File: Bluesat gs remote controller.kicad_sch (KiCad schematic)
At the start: 55 parts, among them J1 USB_C_Receptacle_USB2.0_16P, J2 Conn_01x02, J3 Conn_01x04, J4 Conn_01x04, J5 Conn_01x06, J6 Conn_01x02, SW1 Reset, SW2 Boot, SW3 AZ, SW4 EL, U1 MCP73831-2-OT, U2 AP2112K-3.3, U4 ESP32-S3-WROOM-1

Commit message: Fix battery switch placement and status LED wiring
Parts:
- added SW5: SW_SPDT, symbol Switch:SW_SPDT
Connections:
- net GND: now also C1.1, C3.1, R4.2, U2.1 (VIN), U2.3 (EN), SW5.1 (A); no longer R19.1, R20.1
- net VBAT: now also SW5.2 (B); no longer C1.1, C3.1, R4.2, U2.1 (VIN), U2.3 (EN)
- net LED_STAT1: now reaches U4.17 (IO9)
- net LED_STAT1: now also R19.1
- net LED_STAT2: now reaches U4.18 (IO10)
- net LED_STAT2: now also R20.1
- no-connect marks 2 -> 3
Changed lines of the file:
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@@
-	)
-	(junction
-		(at 113.03 88.9)
-		(diameter 0)
-		(color 0 0 0 0)
 	)
 	(junction
@@
 	)
 	(junction
-		(at 140.97 36.83)
-		(diameter 0)
-		(color 0 0 0 0)
-	)
-	(junction
 		(at 130.81 88.9)
-		(diameter 0)
-		(color 0 0 0 0)
-	)
-	(junction
-		(at 113.03 107.95)
 		(diameter 0)
 		(color 0 0 0 0)
@@
 	)
 	(no_connect
+		(at 85.09 73.66)
+	)
+	(no_connect
 		(at 43.18 82.55)
 	)
@@
 	(wire
 		(pts
-			(xy 106.68 107.95) (xy 113.03 107.95)
-		)
-		(stroke
-			(width 0)
-			(type default)
-		)
-	)
-	(wire
-		(pts
 			(xy 27.94 92.71) (xy 27.94 99.06)
 		)
@@
 	(wire
 		(pts
-			(xy 113.03 88.9) (xy 125.73 88.9)
+			(xy 102.87 88.9) (xy 125.73 88.9)
 		)
 		(stroke
@@
 	(wire
 		(pts
-			(xy 113.03 107.95) (xy 120.65 107.95)
-		)
-		(stroke
-			(width 0)
-			(type default)
-		)
-	)
-	(wire
-		(pts
-			(xy 113.03 88.9) (xy 113.03 107.95)
-		)
-		(stroke
-			(width 0)
-			(type default)
-		)
-	)
-	(wire
-		(pts
 			(xy 148.59 88.9) (xy 148.59 97.79)
 		)
@@
 	(wire
 		(pts
-			(xy 102.87 88.9) (xy 113.03 88.9)
-		)
-		(stroke
-			(width 0)
-			(type default)
-		)
-	)
-	(wire
-		(pts
 			(xy 130.81 102.87) (xy 130.81 101.6)
 		)
@@
 	(wire
 		(pts
-			(xy 140.97 36.83) (xy 157.48 36.83)
+			(xy 134.62 36.83) (xy 157.48 36.83)
 		)
 		(stroke
@@
 	(wire
 		(pts
-			(xy 140.97 40.64) (xy 140.97 36.83)
-		)
-		(stroke
-			(width 0)
-			(type default)
-		)
-	)
-	(wire
-		(pts
 			(xy 140.97 48.26) (xy 140.97 53.34)
 		)
@@
 		(pts
 			(xy 146.05 158.75) (xy 153.67 158.75)
-		)
-		(stroke
-			(width 0)
-			(type default)
-		)
-	)
-	(wire
-		(pts
-			(xy 134.62 36.83) (xy 140.97 36.83)
 		)
 		(stroke
@@
 		)
 	)
+	(label "LED_STAT1"
+		(at 120.65 107.95 0)
+		(effects
+			(font
+				(size 1.27 1.27)
+			)
+			(justify left bottom)
+		)
+	)
 	(label "ENC_EL_A"
 		(at 207.01 137.16 0)
@@
 		)
 	)
+	(label "PWR_FLAG"
+		(at 60.96 88.9 90)
+		(effects
+			(font
+				(size 1.27 1.27)
+			)
+			(justify left bottom)
+		)
+	)
 	(label "USB_D-"
 		(at 63.5 127 180)
@@
 		)
 	)
+	(label "VSYS"
+		(at 85.09 68.58 0)
+		(effects
+			(font
+				(size 1.27 1.27)
+			)
+			(justify left bottom)
+		)
+	)
 	(label "5V"
 		(at 21.59 115.57 0)
@@
 		)
 	)
-	(label "VBAT"
-		(at 52.07 88.9 0)
+	(label "VSYS"
+		(at 52.07 88.9 180)
+		(effects
+			(font
+				(size 1.27 1.27)
+			)
+			(justify right bottom)
+		)
+	)
+	(label "VSYS"
+		(at 140.97 40.64 0)
 		(effects
 			(font
@@
 		)
 	)
+	(label "LED_STAT2"
+		(at 106.68 107.95 0)
+		(effects
+			(font
+				(size 1.27 1.27)
+			)
+			(justify left bottom)
+		)
+	)
 	(label "5V"
 		(at 123.19 63.5 0)
@@
 		)
 	)
+	(label "VBAT"
+		(at 74.93 71.12 180)
+		(effects
+			(font
+				(size 1.27 1.27)
+			)
+			(justify right bottom)
+		)
+	)
 	(label "ENC_EL_SW"
 		(at 245.11 151.13 0)
@@
 		)
 	)
+	(label "LED_STAT2"
+		(at 222.25 76.2 180)
+		(effects
+			(font
+				(size 1.27 1.27)
+			)
+			(justify right bottom)
+		)
+	)
 	(label "ENC_AZ_A"
 		(at 132.08 137.16 0)
@@
 			)
 			(justify left bottom)
+		)
+	)
+	(label "LED_STAT1"
+		(at 222.25 73.66 180)
+		(effects
+			(font
+				(size 1.27 1.27)
+			)
+			(justify right bottom)
 		)
 	)
@@
 					(unit 1)
 				)
+			)
+		)
+	)
+	(symbol
+		(lib_id "Switch:SW_SPDT")
+		(at 80.01 71.12 0)
+		(unit 1)
+		(body_style 1)
+		(exclude_from_sim no)
+		(in_bom yes)
+		(on_board yes)
+		(in_pos_files yes)
+		(dnp no)
+		(fields_autoplaced yes)
+		(property "Reference" "SW5"
+			(at 80.01 62.23 0)
+			(show_name no)
+			(do_not_autoplace no)
+			(effects
+				(font
+					(size 1.27 1.27)
+				)
+			)
+		)
+		(property "Value" "SW_SPDT"
+			(at 80.01 64.77 0)
+			(show_name no)
+			(do_not_autoplace no)
+			(effects
+				(font
+					(size 1.27 1.27)
+				)
+			)
+		)
+		(property "Footprint" ""
+			(at 80.01 71.12 0)
+			(hide yes)
+			(show_name no)
+			(do_not_autoplace no)
+			(effects
+				(font
+					(size 1.27 1.27)
+				)
+			)
+		)
+		(property "Datasheet" ""
+			(at 80.01 78.74 0)
+			(hide yes)
+			(show_name no)
+			(do_not_autoplace no)
+			(effects
+				(font
+					(size 1.27 1.27)
+				)
+			)
+		)
+		(property "Description" "Switch, single pole double throw"
+			(at 80.01 71.12 0)
+			(hide yes)
+			(show_name no)
+			(do_not_autoplace no)
+			(effects
+				(font
+					(size 1.27 1.27)
+				)
+			)
+		)
+		(pin "1"
+		)
+		(pin "3"
+		)
+		(pin "2"
+		)
+		(instances
+			(project "Bluesat gs remote controller"
+				(path "/36e07d47-8f23-4d19-870b-29efa343c1de"
+					(reference "SW5")
+					(unit 1)
+				)

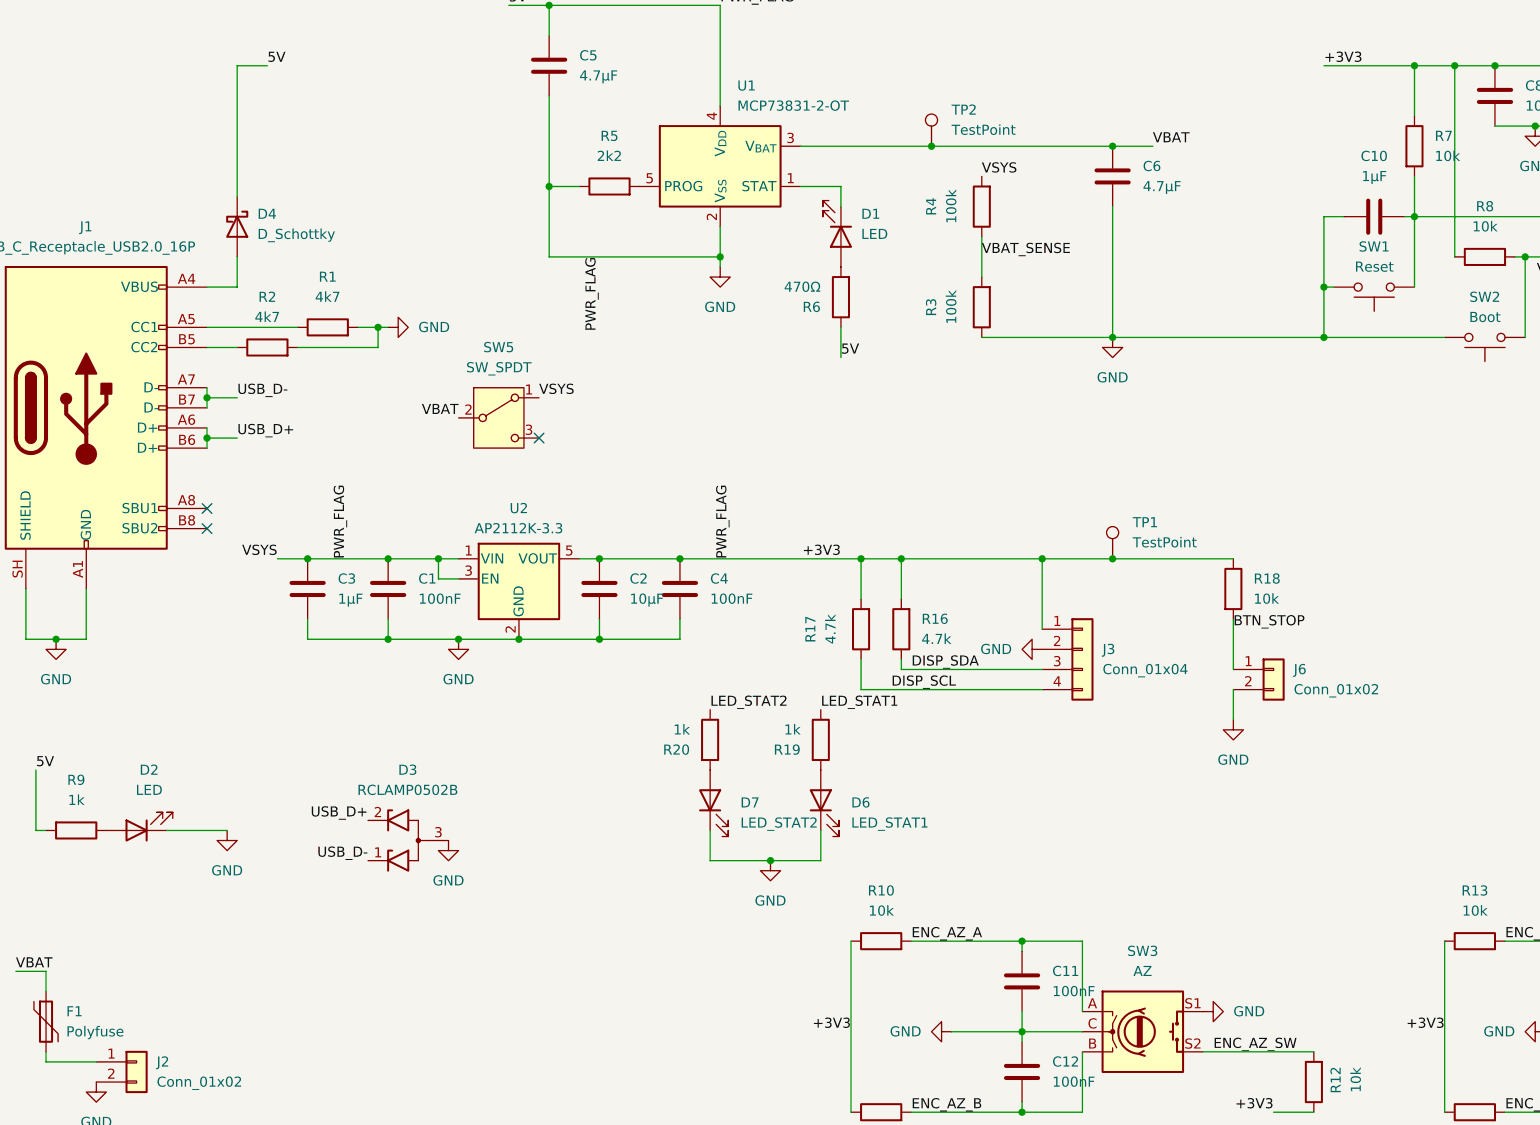
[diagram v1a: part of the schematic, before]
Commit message: Add USB/battery power path
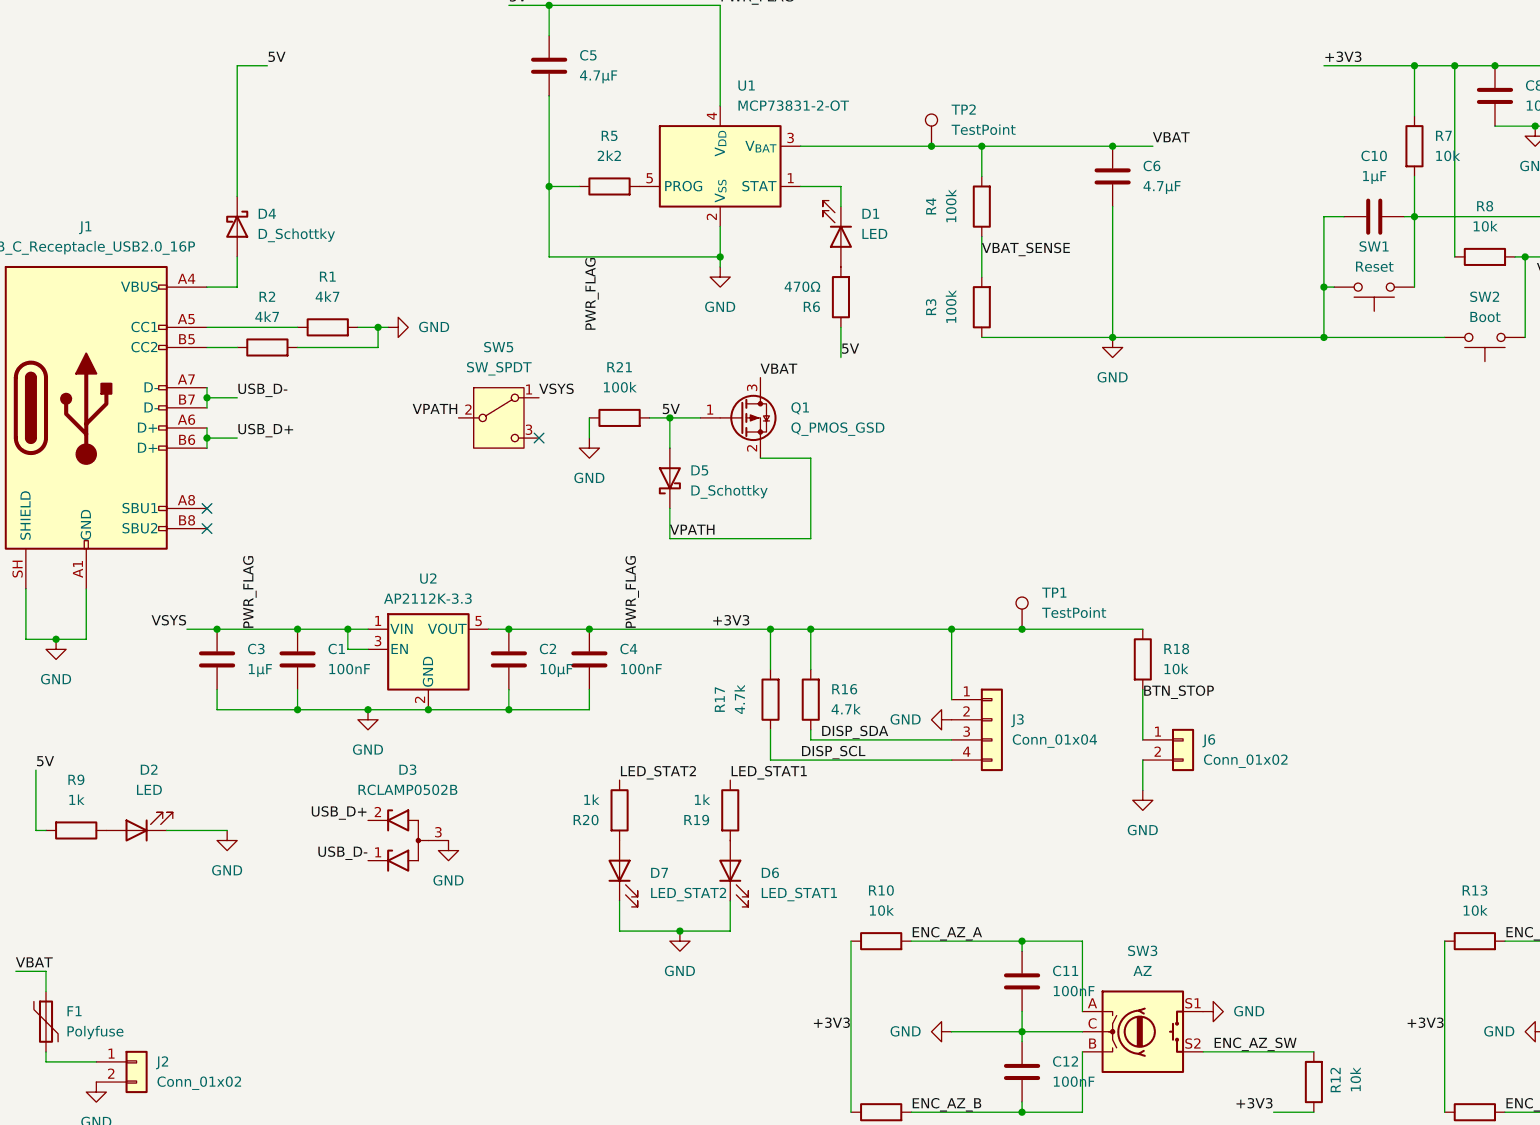
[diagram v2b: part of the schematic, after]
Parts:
- added D5: D_Schottky, Diode_SMD:D_SOD-123, symbol Device:D_Schottky
- added Q1: Q_PMOS_GSD, symbol Transistor_FET:Q_PMOS_GSD
- added R21: 100k, Resistor_SMD:R_0402_1005Metric_Pad0.72x0.64mm_HandSolder, symbol Device:R
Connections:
- net GND: now also D5.2 (A), Q1.1 (G), R21.1, R21.2; no longer R4.2
- net VBAT: now also R4.2, Q1.3 (D); no longer SW5.2 (B)
- new net VPATH: D5.1 (K), Q1.2 (S), SW5.2 (B)
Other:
- moved on the sheet: C1, C2, C3, C4, D6, D7, J3, J6, R16, R17, R18, R19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

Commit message: Add 4 push buttons, regroup schematic, fix R24 and R5 connections
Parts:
- removed C1: 100nF, Capacitor_SMD:C_0402_1005Metric_Pad0.74x0.62mm_HandSolder, symbol Device:C
- removed U2: AP2112K-3.3, Package_TO_SOT_SMD:SOT-23-5, symbol Regulator_Linear:AP2112K-3.3
- added C15, C16, C17, C7: 100nF, Capacitor_SMD:C_1206_3216Metric, symbol Device:C
- added L1: L, Inductor_SMD:L_Taiyo-Yuden_NR-30xx, symbol Device:L
- added R22: 100k, Resistor_SMD:R_0402_1005Metric, symbol Device:R
- added R23: 22k, Resistor_SMD:R_0402_1005Metric, symbol Device:R
- added R24, R25, R26, R27: 10k, Resistor_SMD:R_0402_1005Metric, symbol Device:R
- added SW6, SW7, SW8, SW9: SW_Push, symbol Switch:SW_Push
- added U2: SY8089AAAC, Package_TO_SOT_SMD:SOT-23-5, symbol Regulator_Switching:TLV62569DBV
- C10: footprint Capacitor_SMD:C_0603_1608Metric_Pad1.08x0.95mm_HandSolder -> Capacitor_SMD:C_0603_1608Metric
- C11, C12, C13, C14, C4, C9: footprint Capacitor_SMD:C_0402_1005Metric_Pad0.74x0.62mm_HandSolder -> Capacitor_SMD:C_0402_1005Metric
- C2: value 10µF -> 22µF; footprint Capacitor_SMD:C_1206_3216Metric_Pad1.33x1.80mm_HandSolder -> Capacitor_SMD:C_1206_3216Metric
- C3: value 1µF -> 22µF; footprint Capacitor_SMD:C_0603_1608Metric_Pad1.08x0.95mm_HandSolder -> Capacitor_SMD:C_1206_3216Metric
- C5, C6, C8: footprint Capacitor_SMD:C_1206_3216Metric_Pad1.33x1.80mm_HandSolder -> Capacitor_SMD:C_1206_3216Metric
- D1, D2: footprint LED_SMD:LED_0603_1608Metric_Pad1.05x0.95mm_HandSolder -> LED_SMD:LED_0603_1608Metric
- F1: footprint Resistor_SMD:R_1206_3216Metric_Pad1.30x1.75mm_HandSolder -> Fuse:Fuse_1206_3216Metric
- Q1: footprint (none) -> Package_TO_SOT_SMD:SOT-23
- R1, R10, R11, R12, R13, R14, R15, R16, R17, R18, R19, R2, R20, R21, R3, R4, R5, R6, R7, R8, R9: footprint Resistor_SMD:R_0402_1005Metric_Pad0.72x0.64mm_HandSolder -> Resistor_SMD:R_0402_1005Metric
- SW3, SW4: footprint (none) -> Rotary_Encoder:RotaryEncoder_Alps_EC11E-Switch_Vertical_H20mm
- SW5: footprint (none) -> Button_Switch_SMD:SW_SPDT_PCM12
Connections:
- net GND: now also C15.1, C16.1, C17.2, C7.1, R23.1, SW6.1, SW7.1, SW8.1, SW9.2, U2.2 (GND); no longer C2.2, C3.2, C4.1, C5.2, C8.1, C9.1, D4.1 (K), D5.2 (A), J3.1 (Pin_1), J4.1 (Pin_1), J5.1 (Pin_1), Q1.1 (G), R10.1, R11.1, R12.1, R13.1, R14.1, R15.1, R16.2, R17.2, R18.1, R21.2, R5.1, R6.1, R7.1, R8.1, R9.2, SW5.1 (A), TP1.1, U1.4 (V_{DD}), U4.2 (3V3)
- net BTN_1: now reaches U4.31 (IO38)
- net BTN_1: now also C7.2, R24.1, SW6.2
- net BTN_2: now reaches U4.32 (IO39)
- net BTN_2: now also C15.2, R25.1, SW7.2
- net BTN_3: now reaches U4.33 (IO40)
- net BTN_3: now also C16.2, R26.1, SW8.2
- net BTN_4: now reaches U4.34 (IO41)
- net BTN_4: now also C17.1, R27.1, SW9.1
- new net: L1.1, U2.3 (SW)
- new net +3V3: C3.2, C4.1, C8.1, C9.1, J4.1 (Pin_1), J5.1 (Pin_1), L1.2, R10.1, R11.1, R12.1, R13.1, R14.1, R15.1, R16.2, R17.2, R18.1, R22.2, R24.2, R25.2, R26.2, R27.2, R7.1, R8.1, TP1.1, U4.2 (3V3)
- new net 5V: C5.2, D4.1 (K), D5.2 (A), Q1.1 (G), R21.2, R5.1, R6.1, R9.2, U1.4 (V_{DD})
- new net FB: R22.1, R23.2, U2.5 (FB)
- new net VSYS: C2.2, SW5.1 (A), U2.1 (EN), U2.4 (VIN)
- no-connect marks 3 -> 14
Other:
- moved on the sheet: C10, C2, C5, C8, C9, D1, D2, D3, D4, J1, J3, J5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

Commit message: minor final adjustment
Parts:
- C15, C16, C17, C7: footprint Capacitor_SMD:C_1206_3216Metric -> Capacitor_SMD:C_0402_1005Metric
- D6, D7: footprint LED_SMD:LED_0603_1608Metric_Pad1.05x0.95mm_HandSolder -> LED_SMD:LED_0603_1608Metric
- J2, J6: footprint (none) -> Connector_PinHeader_2.54mm:PinHeader_1x02_P2.54mm_Vertical
- J3, J4: footprint (none) -> Connector_PinHeader_2.54mm:PinHeader_1x04_P2.54mm_Vertical
- J5: footprint (none) -> Connector_PinHeader_1.00mm:PinHeader_1x06_P1.00mm_Vertical
- L1: value L -> 2.2uH
- R16, R17: value 4.7k -> 4k7
- R6: value 470Ω -> 470R
- SW1, SW2: footprint (none) -> Button_Switch_SMD:SW_SPST_PTS645Sx43SMTR92
- SW6, SW7, SW8, SW9: footprint (none) -> Button_Switch_THT:SW_PUSH-12mm
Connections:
- net +3V3 is gone; now on net +3.3V: C3.2, C4.1, C8.1, C9.1, J4.1 (Pin_1), J5.1 (Pin_1), L1.2, R10.1, R11.1, R12.1, R13.1, R14.1, R15.1, R16.2, R17.2, R18.1, R22.2, R24.2, R25.2, R26.2, R27.2, R7.1, R8.1, TP1.1, U4.2 (3V3)
- net +3.3V: now reaches J3.1 (Pin_1)
- net 5V renamed +5V
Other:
- note added: "1. USB Input & Protection"
- note added: "D3 (TVS): place close to J1"
- moved on the sheet: C6, C8, C9, D2, D3, R3, R4, R9, TP2

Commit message: Rotator remote: placement done, pre-routing review
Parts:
- C2, C3: footprint Capacitor_SMD:C_1206_3216Metric -> Capacitor_SMD:C_1210_3225Metric
- J5: footprint Connector_PinHeader_1.00mm:PinHeader_1x06_P1.00mm_Vertical -> Connector_PinHeader_2.54mm:PinHeader_1x06_P2.54mm_Vertical
- L1: footprint Inductor_SMD:L_Taiyo-Yuden_NR-30xx -> Inductor_SMD:L_Changjiang_FXL0630
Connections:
- net +5V: no longer R5.1
- net ENC_AZ_B: now also C12.1; no longer C12.2
- net ENC_EL_B: now also C14.1; no longer C14.2
- net GND: now also C12.2, C13.2, C14.2, R5.1, SW2.1; no longer C12.1, SW2.2
- net VPATH: now also SW5.1 (A); no longer SW5.2 (B)
- net VSYS: now also SW5.2 (B); no longer SW5.1 (A)
- net at R8.2, U4.27 (IO0): now also SW2.2; no longer SW2.1
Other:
- note added: "review purpose of circuit"
- moved on the sheet: C10, C12, C14, C15, C16, C17, C2, C3, C4, C7, L1, R22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
